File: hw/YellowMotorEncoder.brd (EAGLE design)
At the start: 35 x 22.4 mm, 20 parts, among them P1 M1

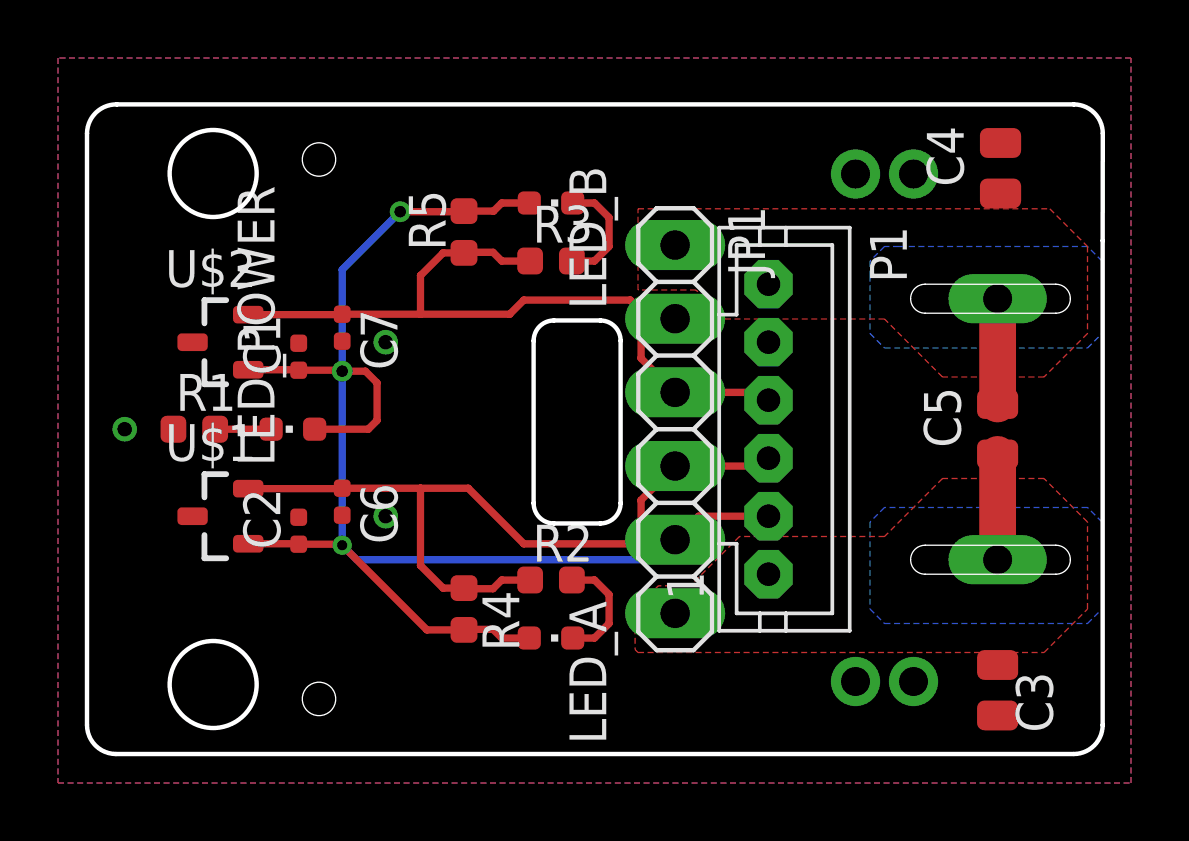
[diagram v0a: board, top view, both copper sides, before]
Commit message: Make many improvements according testing v1.0 and v1.1 boards
- increase version number from v1.1 to v1.2
- decrease width of board from 22.4 to 22.2 mm
- move all parts to corresponding position with respect to the board center
- move hall sensor:
  - Y axis: 0.25 mm closer to the center of board (distance between both sensors is -0.5 mm)
  - X axis: 0.8 mm in motor direction
- improve documetation texts
  - increase size, add some labels
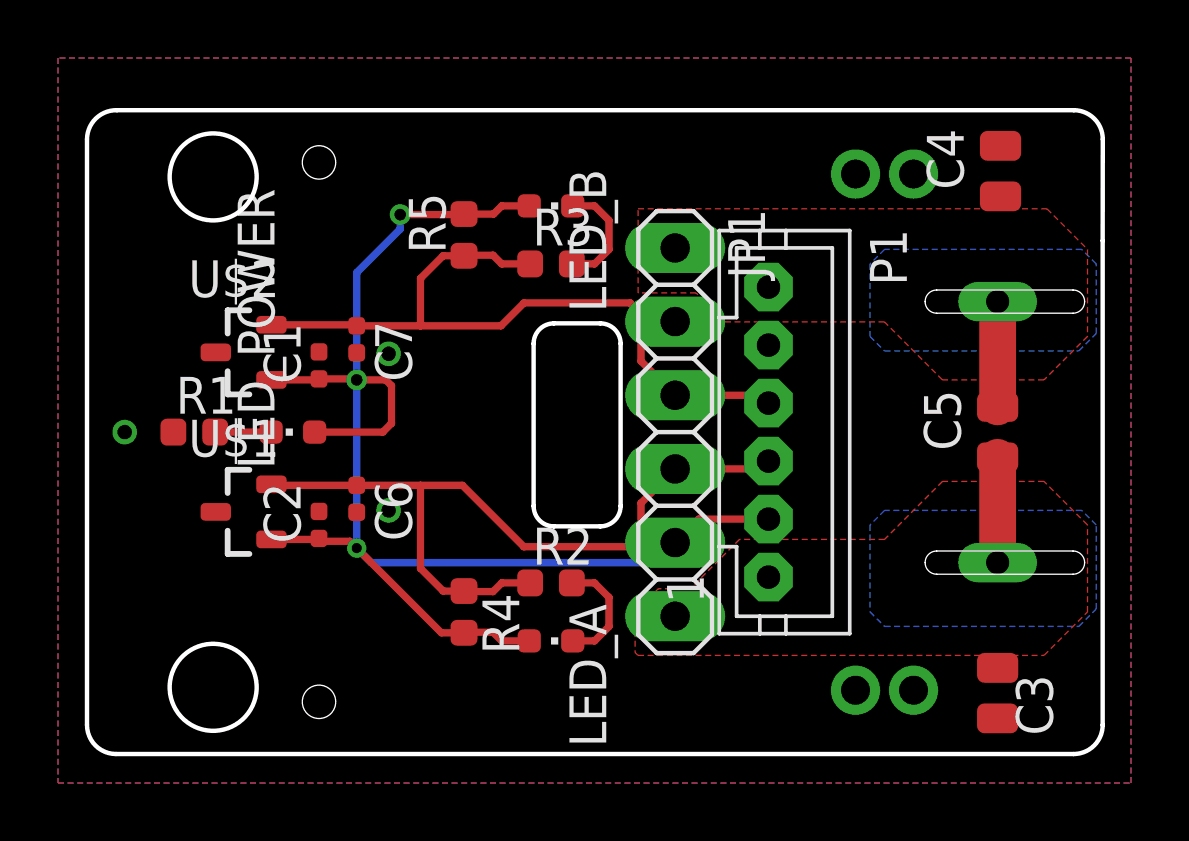
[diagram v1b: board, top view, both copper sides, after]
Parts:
- moved U$2 0.87 mm to (5.40, 13.8)
- moved U$1 0.81 mm to (5.40, 8.35)
- moved C1 0.76 mm to (8.00, 13.4)
- moved C2 0.73 mm to (8.00, 7.90)
- moved C7 0.64 mm to (9.30, 14.3)
- moved C6 0.51 mm to (9.30, 8.80)
- moved LED_B 0.10 mm to (16.0, 18.9)
- moved R3 0.10 mm to (16.0, 16.9)
- moved R5 0.10 mm to (13.0, 17.9)
- moved C3 0.10 mm to (31.4, 2.10)
- moved LED_A 0.10 mm to (16.0, 3.90)
- moved C5 0.10 mm to (31.4, 11.1)
- moved JP1 0.10 mm to (20.3, 11.1)
- moved LED_POWER 0.10 mm to (7.10, 11.1)
- moved P1 0.10 mm to (23.5, 11.1)
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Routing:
- net VCC: track 51.7 -> 50.4 mm
- net A: track 27.5 -> 27.0 mm
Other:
- board size 35 x 22.4 mm -> 35 x 22.2 mm
- board text added: "v1.2 CC BY-SA 4.0"
- board text removed: "v1.1 CC BY-SA 4.0"
